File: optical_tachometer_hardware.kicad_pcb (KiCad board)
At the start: 2 copper layers, 21 x 24 mm, 11 parts, among them J1 J1, Q1 2N2222

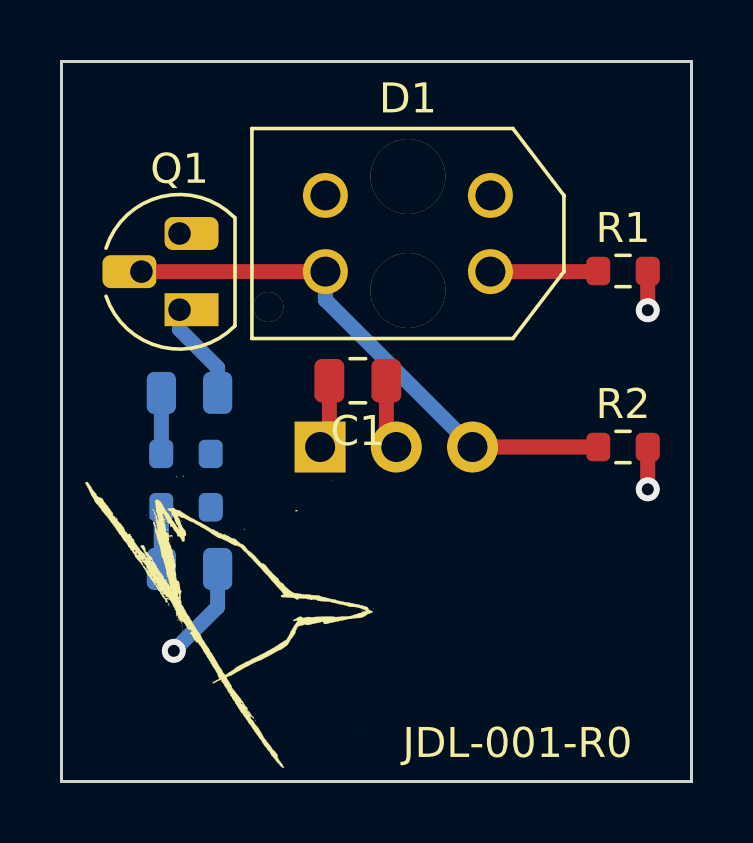
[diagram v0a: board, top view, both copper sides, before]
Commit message: Add descriptive silk
Reduce size (1.0->0.8) of silk text
Reduce silk thickness (0.20->0.15)

Supports #5.
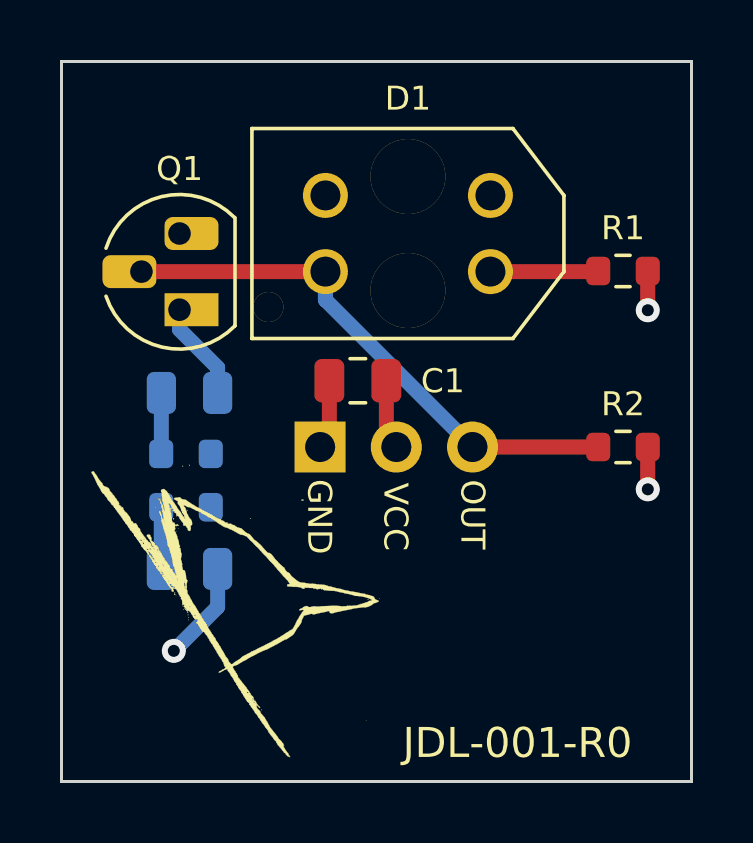
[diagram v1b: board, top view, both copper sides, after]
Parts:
- moved G*** 0.41 mm to (-4.72, 6.45)
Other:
- board text added: "GND"
- board text added: "OUT"
- board text added: "VCC"
